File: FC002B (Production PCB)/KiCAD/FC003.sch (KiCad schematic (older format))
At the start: 55 parts, among them IC1 MSP430G2202, IC10 SC52-11, IC11 SC52-11, IC12 SC52-11, IC2 4017, IC3 74HC4060, IC4 ULN2803A, IC5 SC52-11, IC6 SC52-11, IC7 SC52-11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

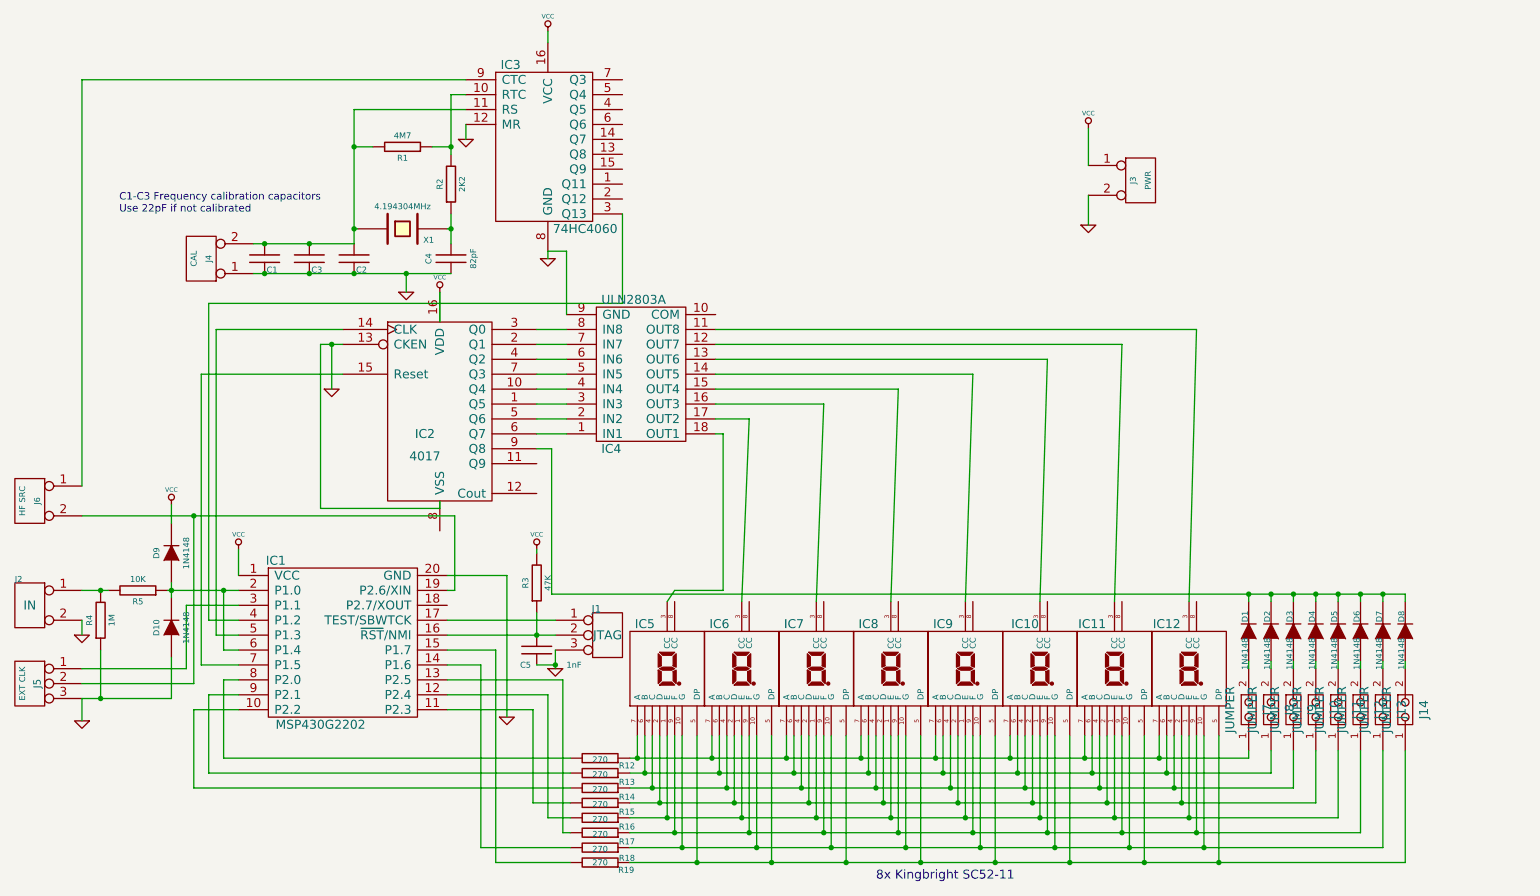
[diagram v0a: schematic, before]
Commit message: FC003 - Hardware bugfix The polarity of the mode select diodes changed the software changed according to the hardware change The schematic improved for the better readability
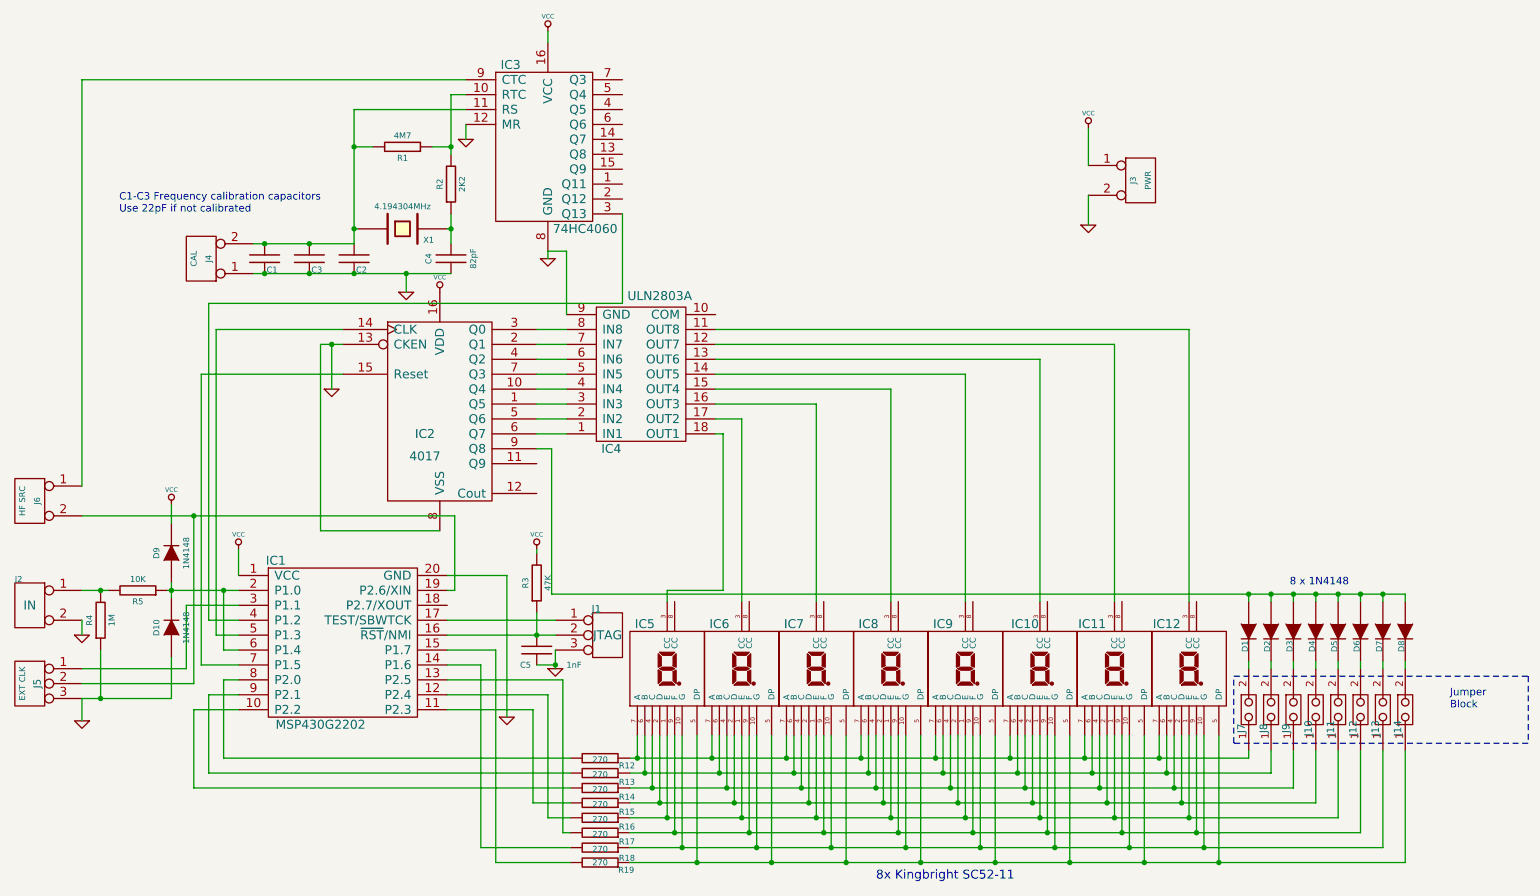
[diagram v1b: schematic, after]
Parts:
- D1, D2, D3, D4, D5, D6, D7, D8: value 1N4148 -> ~
- J10, J11, J12, J13, J14, J7, J8, J9: value JUMPER -> ~
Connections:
- net GND: now also IC2.8 (VSS)
- net at D1.1 (A): now also D2.1 (A), D3.1 (A), D4.1 (A), D5.1 (A), D6.1 (A), D7.1 (A), D8.1 (A), IC2.9 (Q8); no longer J7.2
- net at J8.2: now also D2.2 (K); no longer D2.1 (A)
- net at J9.2: now also D3.2 (K); no longer D3.1 (A)
- net at J10.2: now also D4.2 (K); no longer D4.1 (A)
- net at J11.2: now also D5.2 (K); no longer D5.1 (A)
- net at J12.2: now also D6.2 (K); no longer D6.1 (A)
- net at J13.2: now also D7.2 (K); no longer D7.1 (A)
- net at J14.2: now also D8.2 (K); no longer D8.1 (A)
- new net: D1.2 (K), J7.2
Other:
- note added: "8 x 1N4148"
- note added: "Jumper\nBlock"
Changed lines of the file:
@@
 Sheet 1 1
 Title "FC002B - Frequency Counter"
-Date "3 dec 2013"
+Date "9 jan 2014"
 Rev "1"
 Comp ""
@@
 P 5000 2975
 F 0 "IC4" H 4800 3475 60  0000 C CNN
-F 1 "ULN2803A" H 4950 2475 60  0000 C CNN
+F 1 "ULN2803A" H 5125 2450 60  0000 C CNN
 F 2 "DIP-18__300_ELL" H 5000 2975 60  0001 C CNN
 F 3 "~" H 5000 2975 60  0000 C CNN
@@
 	5550 3375 5550 4425
 Wire Wire Line
-	5550 4425 5225 4425
-Wire Wire Line
-	5225 4425 5175 4500
-Wire Wire Line
-	5500 3275 5725 3275
-Wire Wire Line
-	5725 3275 5675 4500
-Wire Wire Line
-	5500 3175 6225 3175
-Wire Wire Line
-	6225 3175 6175 4500
-Wire Wire Line
-	5500 3075 6725 3075
-Wire Wire Line
-	6725 3075 6675 4500
-Wire Wire Line
-	5500 2975 7225 2975
-Wire Wire Line
-	7225 2975 7175 4500
-Wire Wire Line
-	5500 2875 7725 2875
-Wire Wire Line
-	7725 2875 7675 4500
-Wire Wire Line
-	5500 2775 8225 2775
-Wire Wire Line
-	8225 2775 8175 4500
-Wire Wire Line
-	5500 2675 8725 2675
-Wire Wire Line
-	8725 2675 8675 4500
+	5550 4425 5175 4425
+Wire Wire Line
+	5175 4425 5175 4500
+Wire Wire Line
+	5500 3275 5675 3275
+Wire Wire Line
+	5675 3275 5675 4500
+Wire Wire Line
+	5500 3175 6175 3175
+Wire Wire Line
+	6175 3175 6175 4500
+Wire Wire Line
+	5500 3075 6675 3075
+Wire Wire Line
+	6675 3075 6675 4500
+Wire Wire Line
+	5500 2975 7175 2975
+Wire Wire Line
+	7175 2975 7175 4500
+Wire Wire Line
+	5500 2875 7675 2875
+Wire Wire Line
+	7675 2875 7675 4500
+Wire Wire Line
+	5500 2775 8175 2775
+Wire Wire Line
+	8175 2775 8175 4500
+Wire Wire Line
+	5500 2675 8675 2675
+Wire Wire Line
+	8675 2675 8675 4500
 $Comp
 L 4017 IC2
@@
 P 9075 4700
 F 0 "D1" H 9175 4725 40  0000 C CNN
-F 1 "1N4148" H 8925 4725 40  0000 C CNN
+F 1 "~" H 8925 4725 40  0000 C CNN
 F 2 "D3" H 9075 4700 60  0001 C CNN
 F 3 "" H 9075 4700 60  0000 C CNN
 	1    9075 4700
-	0    -1   -1   0
+	0    -1   1    0
 $EndComp
 $Comp
@@
 P 9225 4700
 F 0 "D2" H 9325 4725 40  0000 C CNN
-F 1 "1N4148" H 9075 4725 40  0000 C CNN
+F 1 "~" H 9075 4725 40  0000 C CNN
 F 2 "D3" H 9225 4700 60  0001 C CNN
 F 3 "" H 9225 4700 60  0000 C CNN
 	1    9225 4700
-	0    -1   -1   0
+	0    -1   1    0
 $EndComp
 $Comp
@@
 P 9375 4700
 F 0 "D3" H 9475 4725 40  0000 C CNN
-F 1 "1N4148" H 9225 4725 40  0000 C CNN
+F 1 "~" H 9225 4725 40  0000 C CNN
 F 2 "D3" H 9375 4700 60  0001 C CNN
 F 3 "" H 9375 4700 60  0000 C CNN
 	1    9375 4700
-	0    -1   -1   0
+	0    -1   1    0
 $EndComp
 $Comp
@@
 P 9525 4700
 F 0 "D4" H 9625 4725 40  0000 C CNN
-F 1 "1N4148" H 9375 4725 40  0000 C CNN
+F 1 "~" H 9375 4725 40  0000 C CNN
 F 2 "D3" H 9525 4700 60  0001 C CNN
 F 3 "" H 9525 4700 60  0000 C CNN
 	1    9525 4700
-	0    -1   -1   0
+	0    -1   1    0
 $EndComp
 $Comp
@@
 P 9675 4700
 F 0 "D5" H 9775 4725 40  0000 C CNN
-F 1 "1N4148" H 9525 4725 40  0000 C CNN
+F 1 "~" H 9525 4725 40  0000 C CNN
 F 2 "D3" H 9675 4700 60  0001 C CNN
 F 3 "" H 9675 4700 60  0000 C CNN
 	1    9675 4700
-	0    -1   -1   0
+	0    -1   1    0
 $EndComp
 $Comp
@@
 P 9825 4700
 F 0 "D6" H 9925 4725 40  0000 C CNN
-F 1 "1N4148" H 9675 4725 40  0000 C CNN
+F 1 "~" H 9675 4725 40  0000 C CNN
 F 2 "D3" H 9825 4700 60  0001 C CNN
 F 3 "" H 9825 4700 60  0000 C CNN
 	1    9825 4700
-	0    -1   -1   0
+	0    -1   1    0
 $EndComp
 $Comp
@@
 P 9975 4700
 F 0 "D7" H 10075 4725 40  0000 C CNN
-F 1 "1N4148" H 9825 4725 40  0000 C CNN
+F 1 "~" H 9825 4725 40  0000 C CNN
 F 2 "D3" H 9975 4700 60  0001 C CNN
 F 3 "" H 9975 4700 60  0000 C CNN
 	1    9975 4700
-	0    -1   -1   0
+	0    -1   1    0
 $EndComp
 $Comp
@@
 P 10125 4700
 F 0 "D8" H 10225 4725 40  0000 C CNN
-F 1 "1N4148" H 9975 4725 40  0000 C CNN
+F 1 "~" H 9975 4725 40  0000 C CNN
 F 2 "D3" H 10125 4700 60  0001 C CNN
 F 3 "" H 10125 4700 60  0000 C CNN
 	1    10125 4700
-	0    -1   -1   0
+	0    -1   1    0
 $EndComp
 Wire Wire Line
@@
 U 1 1 528FD292
 P 9075 5225
-F 0 "J7" V 9200 5225 60  0000 C CNN
-F 1 "JUMPER" V 8950 5225 60  0000 C CNN
+F 0 "J7" V 9025 5100 50  0000 C CNN
+F 1 "~" V 8950 5225 60  0000 C CNN
 F 2 "SIL-2" H 9075 5225 60  0001 C CNN
 F 3 "" H 9075 5225 60  0000 C CNN
@@
 U 1 1 528FD2A1
 P 9225 5225
-F 0 "J8" V 9350 5225 60  0000 C CNN
-F 1 "JUMPER" V 9100 5225 60  0000 C CNN
+F 0 "J8" V 9175 5100 50  0000 C CNN
+F 1 "~" V 9100 5225 60  0000 C CNN
 F 2 "SIL-2" H 9225 5225 60  0001 C CNN
 F 3 "" H 9225 5225 60  0000 C CNN
@@
 U 1 1 528FD2B0
 P 9375 5225
-F 0 "J9" V 9500 5225 60  0000 C CNN
-F 1 "JUMPER" V 9250 5225 60  0000 C CNN
+F 0 "J9" V 9325 5100 50  0000 C CNN
+F 1 "~" V 9250 5225 60  0000 C CNN
 F 2 "SIL-2" H 9375 5225 60  0001 C CNN
 F 3 "" H 9375 5225 60  0000 C CNN
@@
 U 1 1 528FD2BF
 P 9525 5225
-F 0 "J10" V 9650 5225 60  0000 C CNN
-F 1 "JUMPER" V 9400 5225 60  0000 C CNN
+F 0 "J10" V 9475 5100 50  0000 C CNN
+F 1 "~" V 9400 5225 60  0000 C CNN
 F 2 "SIL-2" H 9525 5225 60  0001 C CNN
 F 3 "" H 9525 5225 60  0000 C CNN
@@
 U 1 1 528FD2CE
 P 9675 5225
-F 0 "J11" V 9800 5225 60  0000 C CNN
-F 1 "JUMPER" V 9550 5225 60  0000 C CNN
+F 0 "J11" V 9625 5100 50  0000 C CNN
+F 1 "~" V 9550 5225 60  0000 C CNN
 F 2 "SIL-2" H 9675 5225 60  0001 C CNN
 F 3 "" H 9675 5225 60  0000 C CNN
@@
 U 1 1 528FD2DD
 P 9825 5225
-F 0 "J12" V 9950 5225 60  0000 C CNN
-F 1 "JUMPER" V 9700 5225 60  0000 C CNN
+F 0 "J12" V 9775 5100 50  0000 C CNN
+F 1 "~" V 9700 5225 60  0000 C CNN
 F 2 "SIL-2" H 9825 5225 60  0001 C CNN
 F 3 "" H 9825 5225 60  0000 C CNN
@@
 U 1 1 528FD2EC
 P 9975 5225
-F 0 "J13" V 10100 5225 60  0000 C CNN
-F 1 "JUMPER" V 9850 5225 60  0000 C CNN
+F 0 "J13" V 9925 5100 50  0000 C CNN
+F 1 "~" V 9850 5225 60  0000 C CNN
 F 2 "SIL-2" H 9975 5225 60  0001 C CNN
 F 3 "" H 9975 5225 60  0000 C CNN
@@
 U 1 1 528FD2FB
 P 10125 5225
-F 0 "J14" V 10250 5225 60  0000 C CNN
-F 1 "JUMPER" V 10000 5225 60  0000 C CNN
+F 0 "J14" V 10075 5100 50  0000 C CNN
+F 1 "~" V 10000 5225 60  0000 C CNN
 F 2 "SIL-2" H 10125 5225 60  0001 C CNN
 F 3 "" H 10125 5225 60  0000 C CNN
@@
 	4500 2150 4500 2575
 Wire Wire Line
-	3650 3825 3650 3875
-Wire Wire Line
-	3650 3875 2850 3875
-Wire Wire Line
-	2850 3875 2850 2775
+	3650 4025 2850 4025
+Wire Wire Line
+	2850 4025 2850 2775
 Connection ~ 2925 2775
 $Comp
@@
 	1    0    0    -1
 $EndComp
-Wire Wire Line
-	3650 2425 3650 2625
+Text Notes 9350 4400 0    50   ~ 0
+8 x 1N4148
+Wire Notes Line
+	8975 5000 10950 5000
+Wire Notes Line
+	10950 5000 10950 5450
+Wire Notes Line
+	10950 5450 8975 5450
+Wire Notes Line
+	8975 5450 8975 5000
+Text Notes 10425 5225 0    50   ~ 0
+Jumper\nBlock
 $EndSCHEMATC
